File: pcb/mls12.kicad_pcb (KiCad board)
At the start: 4 copper layers, 80 x 40 mm, 0 parts

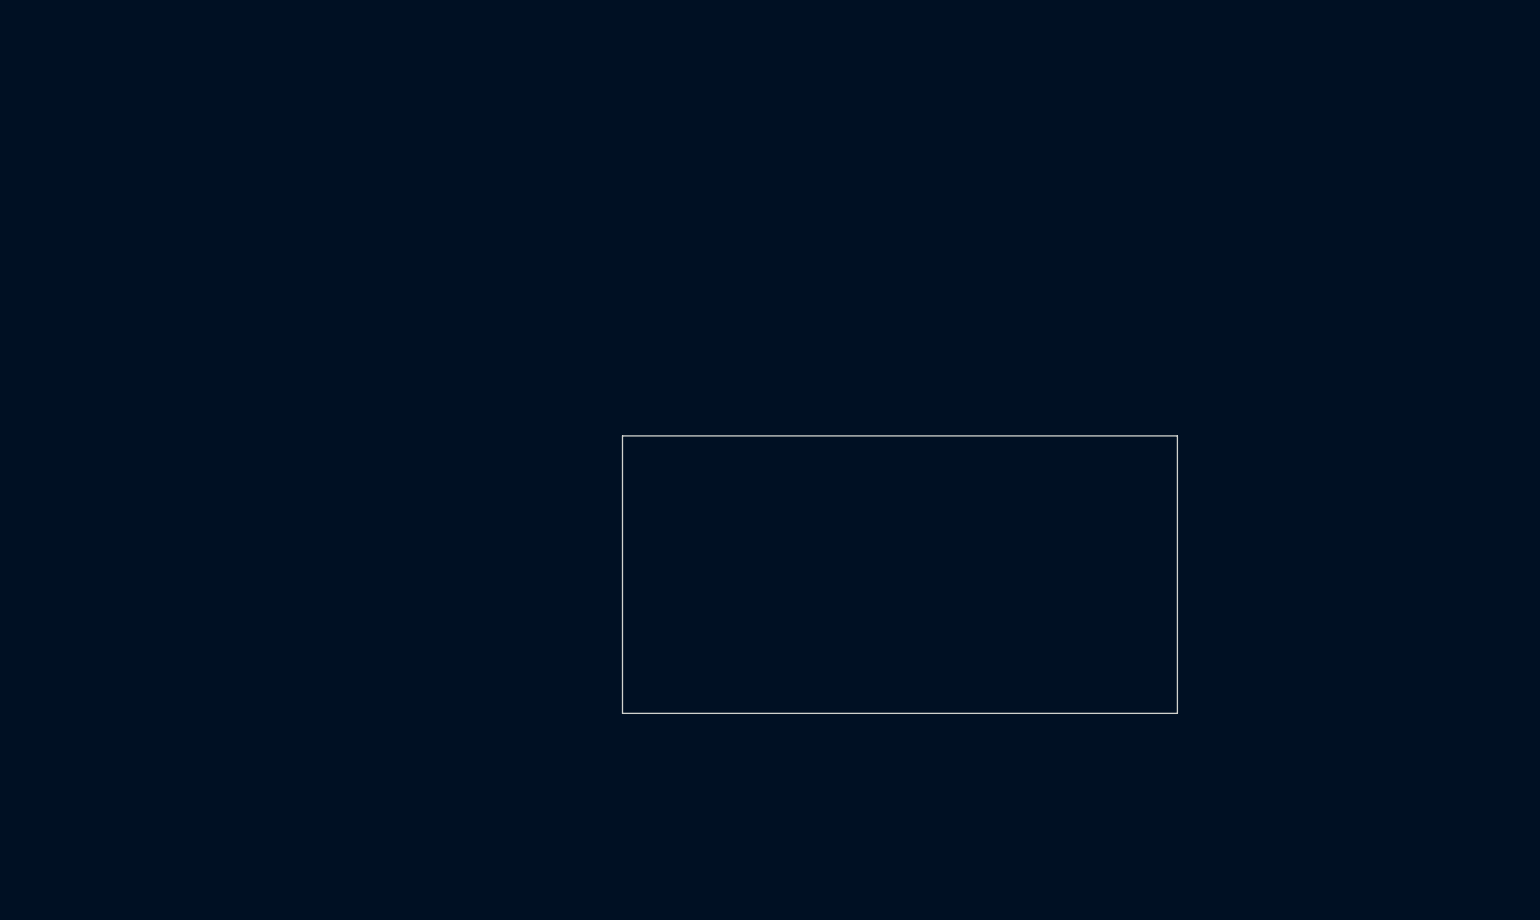
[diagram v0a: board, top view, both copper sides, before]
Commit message: Layout LED outputs, I2C connector
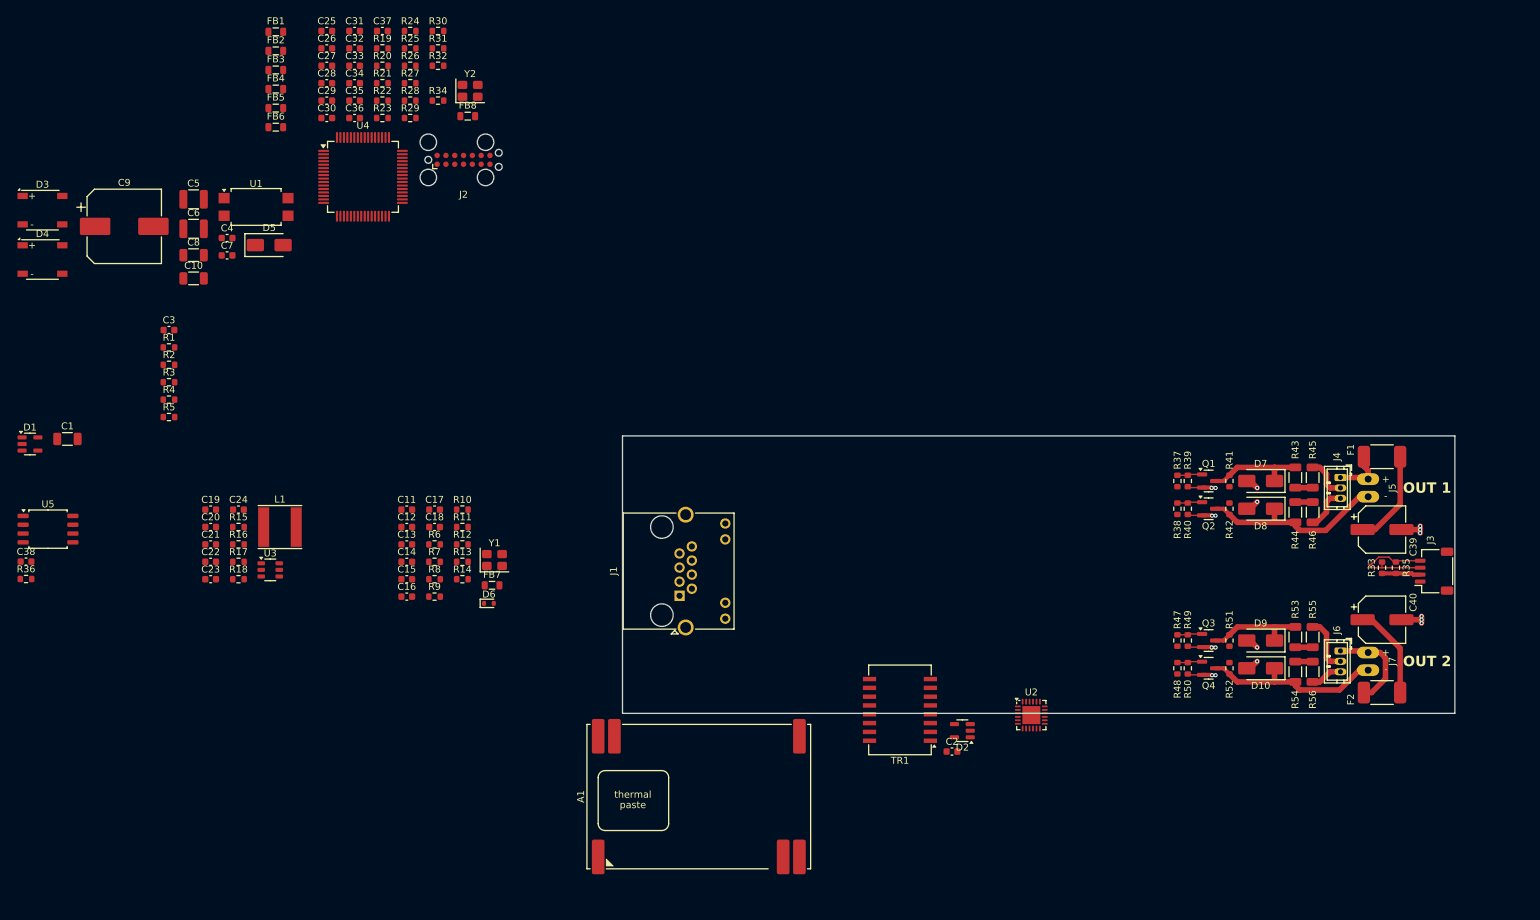
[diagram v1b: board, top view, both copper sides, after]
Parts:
- added A1: Ag5724-LPB, mls12:Ag5724-LPB, F.Cu at (121.0, 132.0)
- added C1: 1000pF/2kV, Capacitor_SMD:C_1206_3216Metric, F.Cu at (30.0, 80.4)
- added C10: 10uF/50V, Capacitor_SMD:C_1206_3216Metric, F.Cu at (48.2, 57.3)
- added C11: 22uF, Capacitor_SMD:C_0603_1608Metric, F.Cu at (78.9, 90.6)
- added C12: 0.1uF, Capacitor_SMD:C_0603_1608Metric, F.Cu at (78.9, 93.1)
- added C13: 0.1uF, Capacitor_SMD:C_0603_1608Metric, F.Cu at (78.9, 95.6)
- added C14: 0.1uF, Capacitor_SMD:C_0603_1608Metric, F.Cu at (78.9, 98.2)
- added C15: 22uF, Capacitor_SMD:C_0603_1608Metric, F.Cu at (78.9, 100.7)
- added C16: 2.2uF, Capacitor_SMD:C_0603_1608Metric, F.Cu at (78.9, 103.2)
- added C17: 10pF, Capacitor_SMD:C_0603_1608Metric, F.Cu at (82.9, 90.6)
- added C18: 10pF, Capacitor_SMD:C_0603_1608Metric, F.Cu at (82.9, 93.1)
- added C19: 4.7uF/35V, Capacitor_SMD:C_0603_1608Metric, F.Cu at (50.6, 90.6)
- added C2: 0.1uF, Capacitor_SMD:C_0603_1608Metric, F.Cu at (157.5, 125.5)
- added C20: 4.7uF/35V, Capacitor_SMD:C_0603_1608Metric, F.Cu at (50.6, 93.1)
- added C21: 0.1uF/50V, Capacitor_SMD:C_0603_1608Metric, F.Cu at (50.6, 95.6)
- added C22: 0.1uF, Capacitor_SMD:C_0603_1608Metric, F.Cu at (50.6, 98.2)
- added C23: 22uF, Capacitor_SMD:C_0603_1608Metric, F.Cu at (50.6, 100.7)
- added C24: 22uF, Capacitor_SMD:C_0603_1608Metric, F.Cu at (54.6, 90.6)
- added C25: 2.2uF, Capacitor_SMD:C_0603_1608Metric, F.Cu at (67.4, 21.6)
- added C26: 2.2uF, Capacitor_SMD:C_0603_1608Metric, F.Cu at (67.4, 24.1)
- added C27: 2.2uF, Capacitor_SMD:C_0603_1608Metric, F.Cu at (67.4, 26.6)
- added C28: 0.1uF, Capacitor_SMD:C_0603_1608Metric, F.Cu at (67.4, 29.1)
- added C29: 0.1uF, Capacitor_SMD:C_0603_1608Metric, F.Cu at (67.4, 31.7)
- added C3: 0.1uF, Capacitor_SMD:C_0603_1608Metric, F.Cu at (44.6, 64.7)
- added C30: 0.1uF, Capacitor_SMD:C_0603_1608Metric, F.Cu at (67.4, 34.2)
- added C31: 0.1uF, Capacitor_SMD:C_0603_1608Metric, F.Cu at (71.4, 21.6)
- added C32: 0.1uF, Capacitor_SMD:C_0603_1608Metric, F.Cu at (71.4, 24.1)
- added C33: 2.2uF, Capacitor_SMD:C_0603_1608Metric, F.Cu at (71.4, 26.6)
- added C34: 2.2uF, Capacitor_SMD:C_0603_1608Metric, F.Cu at (71.4, 29.1)
- added C35: 0.1uF, Capacitor_SMD:C_0603_1608Metric, F.Cu at (71.4, 31.7)
- added C36: 10pF, Capacitor_SMD:C_0603_1608Metric, F.Cu at (71.4, 34.2)
- added C37: 10pF, Capacitor_SMD:C_0603_1608Metric, F.Cu at (75.4, 21.6)
- added C38: 0.1uF, Capacitor_SMD:C_0603_1608Metric, F.Cu at (24.0, 98.1)
- added C39: 100uF/35V, Capacitor_SMD:CP_Elec_6.3x5.9, F.Cu at (219.5, 93.5)
- added C4: 10nF/100V, Capacitor_SMD:C_0603_1608Metric, F.Cu at (53.0, 51.5)
- added C40: 100uF/35V, Capacitor_SMD:CP_Elec_6.3x5.9, F.Cu at (219.5, 106.5)
- added C5: 4.7nF/2kV, Capacitor_SMD:C_1210_3225Metric, F.Cu at (48.2, 45.9)
- added C6: 4.7nF/2kV, Capacitor_SMD:C_1210_3225Metric, F.Cu at (48.2, 50.1)
- added C7: 0.1uF/50V, Capacitor_SMD:C_0603_1608Metric, F.Cu at (53.0, 54.0)
- added C8: 10uF/50V, Capacitor_SMD:C_1206_3216Metric, F.Cu at (48.2, 53.9)
- added C9: 560uF/35V, Capacitor_SMD:CP_Elec_10x10.5, F.Cu at (38.2, 49.8)
- added D1: ESDS312DBV, Package_TO_SOT_SMD:SOT-23-5, F.Cu at (24.6, 81.2)
- added D10: SMAJ24A, Diode_SMD:D_SMA, F.Cu at (202.0, 113.5)
- added D2: ESDS312DBV, Package_TO_SOT_SMD:SOT-23-5, F.Cu at (159.0, 122.5)
- added D3: LMB110S-TP, mls12:LMB110S-TP, F.Cu at (26.4, 47.5)
- added D4: LMB110S-TP, mls12:LMB110S-TP, F.Cu at (26.4, 54.6)
- added D5: SMAJ58A, Diode_SMD:D_SMA, F.Cu at (59.1, 52.5)
- added D6: 1N4148, Diode_SMD:D_SOD-523, F.Cu at (90.7, 104.1)
- added D7: SMAJ24A, Diode_SMD:D_SMA, F.Cu at (202.0, 86.5)
- added D8: SMAJ24A, Diode_SMD:D_SMA, F.Cu at (202.0, 90.5)
- added D9: SMAJ24A, Diode_SMD:D_SMA, F.Cu at (202.0, 109.5)
- added F1: 500mA/30V, mls12:SMD1812B050TF_30, F.Cu at (219.5, 83.0)
- added F2: 500mA/30V, mls12:SMD1812B050TF_30, F.Cu at (219.5, 117.0)
- added FB1: FerriteBead_Small, Inductor_SMD:L_0805_2012Metric, F.Cu at (60.0, 21.7)
- added FB2: FerriteBead_Small, Inductor_SMD:L_0805_2012Metric, F.Cu at (60.0, 24.5)
- added FB3: FerriteBead_Small, Inductor_SMD:L_0805_2012Metric, F.Cu at (60.0, 27.2)
- added FB4: FerriteBead_Small, Inductor_SMD:L_0805_2012Metric, F.Cu at (60.0, 30.0)
- added FB5: FerriteBead_Small, Inductor_SMD:L_0805_2012Metric, F.Cu at (60.0, 32.7)
- added FB6: FerriteBead_Small, Inductor_SMD:L_0805_2012Metric, F.Cu at (60.0, 35.5)
- added FB7: FerriteBead_Small, Inductor_SMD:L_0805_2012Metric, F.Cu at (91.2, 101.5)
- added FB8: FerriteBead_Small, Inductor_SMD:L_0805_2012Metric, F.Cu at (87.7, 33.9)
- added J1: MTJ-88ARX1-FSM-LG, Connector_RJ:RJ45_Amphenol_RJHSE538X, F.Cu at (118.2, 103.0)
- added J2: TC2070-FP, Connector:Tag-Connect_TC2070-IDC-FP_2x07_P1.27mm_Vertical, F.Cu at (87.1, 40.2)
- added J3: SM04B-SRSS-TB, Connector_JST:JST_SH_SM04B-SRSS-TB_1x04-1MP_P1.00mm_Horizontal, F.Cu at (227.0, 99.5)
- added J4: JST B3B-ZR, Connector_JST:JST_ZH_B3B-ZR_1x03_P1.50mm_Vertical, F.Cu at (213.5, 86.0)
- added J5: DC barrel plug, mls12:DC_Barrel_Plug_2.1x5.5mm, F.Cu at (217.5, 87.5)
- added J6: JST B3B-ZR, Connector_JST:JST_ZH_B3B-ZR_1x03_P1.50mm_Vertical, F.Cu at (213.5, 111.0)
- added J7: DC barrel plug, mls12:DC_Barrel_Plug_2.1x5.5mm, F.Cu at (217.5, 112.5)
- added L1: 33uH, Inductor_SMD:L_Taiyo-Yuden_NR-60xx, F.Cu at (60.6, 93.1)
- added Q1: DMG3406L, Package_TO_SOT_SMD:SOT-23, F.Cu at (194.5, 86.5)
- added Q2: DMG3406L, Package_TO_SOT_SMD:SOT-23, F.Cu at (194.5, 90.5)
- added Q3: DMG3406L, Package_TO_SOT_SMD:SOT-23, F.Cu at (194.5, 109.5)
- added Q4: DMG3406L, Package_TO_SOT_SMD:SOT-23, F.Cu at (194.5, 113.5)
- added R1: 220R, Resistor_SMD:R_0603_1608Metric, F.Cu at (44.6, 67.2)
- added R10: 33R, Resistor_SMD:R_0603_1608Metric, F.Cu at (86.9, 90.6)
- added R11: 0R, Resistor_SMD:R_0603_1608Metric, F.Cu at (86.9, 93.1)
- added R12: 0R, Resistor_SMD:R_0603_1608Metric, F.Cu at (86.9, 95.6)
- added R13: 1K, Resistor_SMD:R_0603_1608Metric, F.Cu at (86.9, 98.2)
- added R14: 10K, Resistor_SMD:R_0603_1608Metric, F.Cu at (86.9, 100.7)
- added R15: 0R, Resistor_SMD:R_0603_1608Metric, F.Cu at (54.6, 93.1)
- added R16: ~, Resistor_SMD:R_0603_1608Metric, F.Cu at (54.6, 95.6)
- added R17: 100K/1%, Resistor_SMD:R_0603_1608Metric, F.Cu at (54.6, 98.2)
- added R18: 32K/1%, Resistor_SMD:R_0603_1608Metric, F.Cu at (54.6, 100.7)
- added R19: 1K, Resistor_SMD:R_0603_1608Metric, F.Cu at (75.4, 24.1)
- added R2: 75, Resistor_SMD:R_0603_1608Metric, F.Cu at (44.6, 69.8)
- added R20: 33R, Resistor_SMD:R_0603_1608Metric, F.Cu at (75.4, 26.6)
- added R21: 33R, Resistor_SMD:R_0603_1608Metric, F.Cu at (75.4, 29.1)
- added R22: 10K, Resistor_SMD:R_0603_1608Metric, F.Cu at (75.4, 31.7)
- added R23: 33R, Resistor_SMD:R_0603_1608Metric, F.Cu at (75.4, 34.2)
- added R24: 33R, Resistor_SMD:R_0603_1608Metric, F.Cu at (79.4, 21.6)
- added R25: 33R, Resistor_SMD:R_0603_1608Metric, F.Cu at (79.4, 24.1)
- added R26: 33R, Resistor_SMD:R_0603_1608Metric, F.Cu at (79.4, 26.6)
- added R27: 0R, Resistor_SMD:R_0603_1608Metric, F.Cu at (79.4, 29.1)
- added R28: 100R, Resistor_SMD:R_0603_1608Metric, F.Cu at (79.4, 31.7)
- added R29: 100R, Resistor_SMD:R_0603_1608Metric, F.Cu at (79.4, 34.2)
- added R3: 75, Resistor_SMD:R_0603_1608Metric, F.Cu at (44.6, 72.3)
- added R30: 100R, Resistor_SMD:R_0603_1608Metric, F.Cu at (83.4, 21.6)
- added R31: 100R, Resistor_SMD:R_0603_1608Metric, F.Cu at (83.4, 24.1)
- added R32: 100R, Resistor_SMD:R_0603_1608Metric, F.Cu at (83.4, 26.6)
- added R33: 4K7, Resistor_SMD:R_0603_1608Metric, F.Cu at (219.5, 99.0)
- added R34: 100R, Resistor_SMD:R_0603_1608Metric, F.Cu at (83.4, 31.7)
- added R35: 4K7, Resistor_SMD:R_0603_1608Metric, F.Cu at (221.5, 99.0)
- added R36: 10K, Resistor_SMD:R_0603_1608Metric, F.Cu at (24.0, 100.6)
- added R37: 100R, Resistor_SMD:R_0603_1608Metric, F.Cu at (190.0, 86.5)
- added R38: 100R, Resistor_SMD:R_0603_1608Metric, F.Cu at (190.0, 90.5)
- added R39: 10K, Resistor_SMD:R_0603_1608Metric, F.Cu at (191.5, 86.5)
- added R4: 75, Resistor_SMD:R_0603_1608Metric, F.Cu at (44.6, 74.8)
- added R40: 10K, Resistor_SMD:R_0603_1608Metric, F.Cu at (191.5, 90.5)
- added R41: 10K, Resistor_SMD:R_0603_1608Metric, F.Cu at (197.5, 86.5)
- added R42: 10K, Resistor_SMD:R_0603_1608Metric, F.Cu at (197.5, 90.5)
- added R43: 3R/750mW, Resistor_SMD:R_1206_3216Metric, F.Cu at (207.0, 86.0)
- added R44: 3R/750mW, Resistor_SMD:R_1206_3216Metric, F.Cu at (207.0, 91.0)
- added R45: 3R/750mW, Resistor_SMD:R_1206_3216Metric, F.Cu at (209.5, 86.0)
- added R46: 3R/750mW, Resistor_SMD:R_1206_3216Metric, F.Cu at (209.5, 91.0)
- added R47: 100R, Resistor_SMD:R_0603_1608Metric, F.Cu at (190.0, 109.5)
- added R48: 100R, Resistor_SMD:R_0603_1608Metric, F.Cu at (190.0, 113.5)
- added R49: 10K, Resistor_SMD:R_0603_1608Metric, F.Cu at (191.5, 109.5)
- added R5: 75, Resistor_SMD:R_0603_1608Metric, F.Cu at (44.6, 77.3)
- added R50: 10K, Resistor_SMD:R_0603_1608Metric, F.Cu at (191.5, 113.5)
- added R51: 10K, Resistor_SMD:R_0603_1608Metric, F.Cu at (197.5, 109.5)
- added R52: 10K, Resistor_SMD:R_0603_1608Metric, F.Cu at (197.5, 113.5)
- added R53: 3R/750mW, Resistor_SMD:R_1206_3216Metric, F.Cu at (207.0, 109.0)
- added R54: 3R/750mW, Resistor_SMD:R_1206_3216Metric, F.Cu at (207.0, 114.0)
- added R55: 3R/750mW, Resistor_SMD:R_1206_3216Metric, F.Cu at (209.5, 109.0)
- added R56: 3R/750mW, Resistor_SMD:R_1206_3216Metric, F.Cu at (209.5, 114.0)
- added R6: 6K49/1%, Resistor_SMD:R_0603_1608Metric, F.Cu at (82.9, 95.6)
- added R7: 33R, Resistor_SMD:R_0603_1608Metric, F.Cu at (82.9, 98.2)
- added R8: 33R, Resistor_SMD:R_0603_1608Metric, F.Cu at (82.9, 100.7)
- added R9: 33R, Resistor_SMD:R_0603_1608Metric, F.Cu at (82.9, 103.2)
- added TR1: 7490120110, mls12:7490120110, F.Cu at (150.0, 119.5)
- added U1: DPC817S-C-TR, mls12:DPC817S-C-TR, F.Cu at (57.2, 47.0)
- added U2: KSZ8081RNA, Package_DFN_QFN:QFN-24-1EP_4x4mm_P0.5mm_EP2.6x2.6mm, F.Cu at (168.9, 120.2)
- added U3: LMR51606XDBVR, mls12:LMR51606_SOT-23-6, F.Cu at (59.2, 99.3)
- added U4: STM32H563RIT6, Package_QFP:LQFP-64_10x10mm_P0.5mm, F.Cu at (72.6, 42.6)
- added U5: W25Q16JVSS, Package_SO:SOIC-8_5.3x5.3mm_P1.27mm, F.Cu at (27.2, 93.4)
- added Y1: 25MHz, Crystal:Crystal_SMD_3225-4Pin_3.2x2.5mm, F.Cu at (91.5, 97.9)
- added Y2: 25MHz, Crystal:Crystal_SMD_3225-4Pin_3.2x2.5mm, F.Cu at (88.0, 30.2)
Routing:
- net GND: track 0.00 -> 30.7 mm, vias 0 -> 18
- net /LED output 1/LED_CW-: track 0.00 -> 28.1 mm
- net +24V: track 0.00 -> 27.3 mm
- net /LED output 2/LED_CW-: track 0.00 -> 27.3 mm
- net /LED output 2/LED_WW-: track 0.00 -> 14.3 mm
- net /LED output 1/LED_WW-: track 0.00 -> 14.3 mm
- net /LED output 2/LED+: track 0.00 -> 13.9 mm
- net /MCU/SDA: track 0.00 -> 8.33 mm
- net /MCU/SCL: track 0.00 -> 8.30 mm
- net Net-(J6-Pin_2): track 0.00 -> 8.11 mm
- net /LED output 1/LED+: track 0.00 -> 7.58 mm
- net Net-(J4-Pin_3): track 0.00 -> 6.31 mm
- net Net-(J4-Pin_2): track 0.00 -> 6.11 mm
- net +3.3V: track 0.00 -> 5.57 mm
- net Net-(J6-Pin_3): track 0.00 -> 4.61 mm
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- added copper zone on In1.Cu, net GND
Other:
- board size 80 x 40 mm -> 120 x 40 mm
- board text added: "OUT 1"
- board text added: "OUT 2"

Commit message: First Ethernet frontend layout
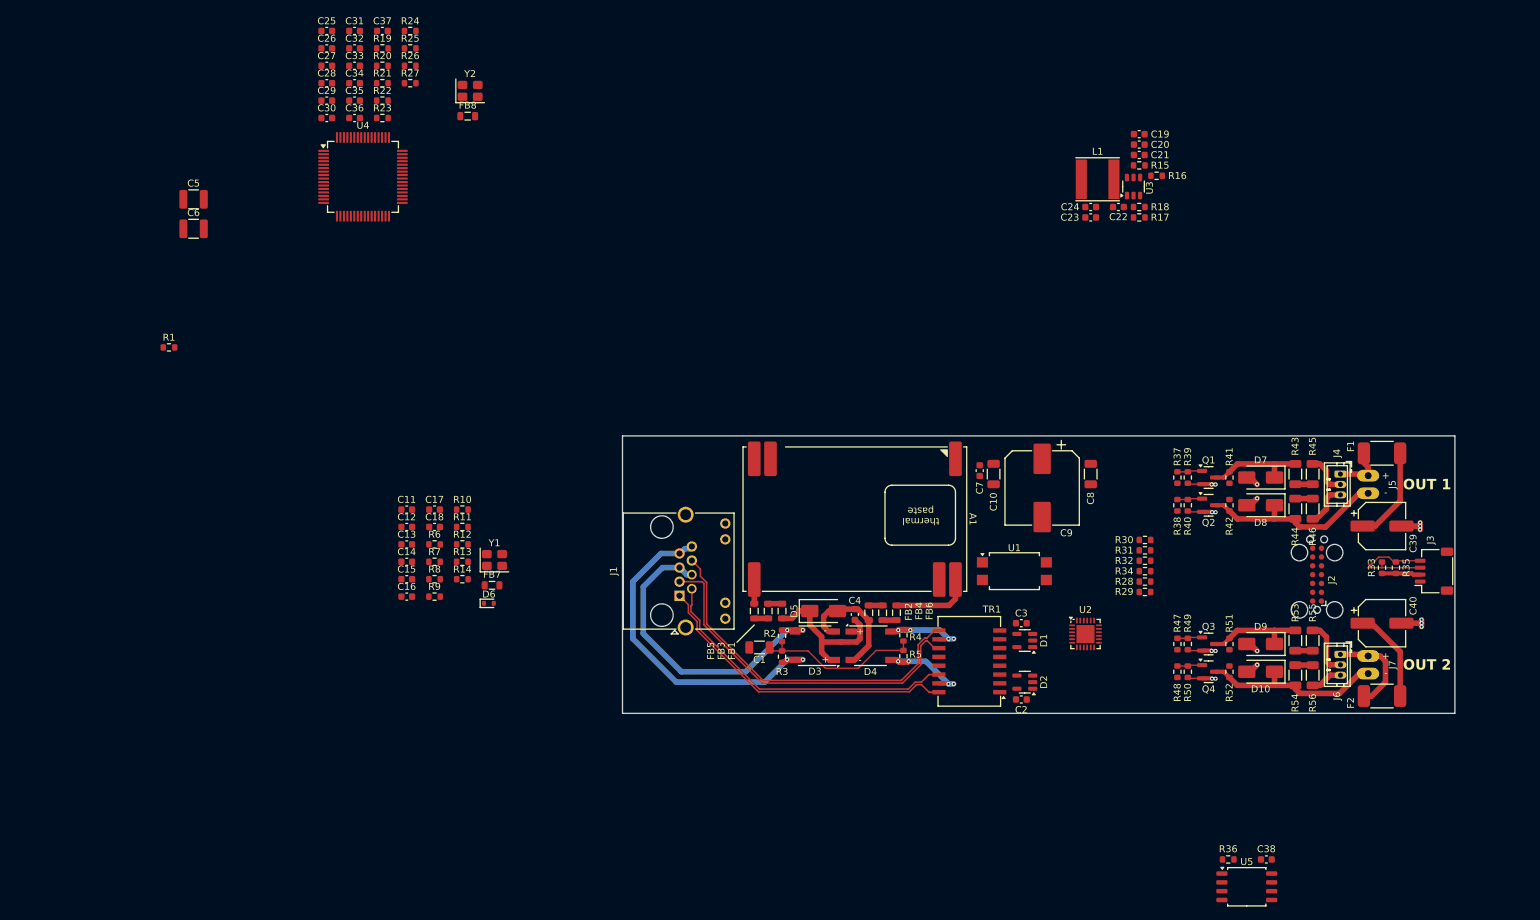
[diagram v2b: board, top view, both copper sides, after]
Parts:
- moved C38 183.9 mm to (202.8, 141.1), turned to 180 degrees
- moved U5 180.4 mm to (200.0, 145.0)
- moved R36 178.0 mm to (197.3, 141.1), turned to 180 degrees
- moved D1 146.2 mm to (168.0, 109.5), turned to 180 degrees
- moved C21 145.2 mm to (184.5, 39.5)
- moved C20 144.8 mm to (184.5, 38.0)
- moved C19 144.4 mm to (184.5, 36.5)
- moved R16 142.6 mm to (187.0, 42.5)
- moved C22 140.5 mm to (181.5, 47.0), turned to 180 degrees
- moved R18 140.5 mm to (184.5, 47.0), turned to 180 degrees
- moved R15 139.9 mm to (184.5, 41.0)
- moved R17 139.0 mm to (184.5, 48.5)
- moved C9 137.6 mm to (170.5, 87.5), turned to -90 degrees
- moved C23 137.2 mm to (177.5, 48.5)
- moved J2 136.8 mm to (210.1, 100.0), turned to 90 degrees
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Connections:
- net /ETH-CONN/RX+ renamed /ETH-CONN/MDI_RD+
- net /ETH-CONN/RX- renamed /ETH-CONN/MDI_RD-
- net /ETH-CONN/TX+ renamed /ETH-CONN/MDI_TD+
- net /ETH-CONN/TX- renamed /ETH-CONN/MDI_TD-
- net Net-(TR1-RX+) renamed /ETH-CONN/MDI_RX+
- net Net-(TR1-RX-) renamed /ETH-CONN/MDI_RX-
- net Net-(TR1-TX+) renamed /ETH-CONN/MDI_TX+
- net Net-(TR1-TX-) renamed /ETH-CONN/MDI_TX-
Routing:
- net /ETH-CONN/MDI_RX+: track 0.00 -> 51.5 mm
- net /ETH-CONN/MDI_RX-: track 0.00 -> 51.5 mm
- net /ETH-CONN/V_{INB}: track 0.00 -> 50.5 mm, vias 0 -> 2
- net /ETH-CONN/V_{INA}: track 0.00 -> 46.3 mm, vias 0 -> 2
- net /ETH-CONN/MDI_TX+: track 0.00 -> 45.4 mm
- net /ETH-CONN/MDI_TX-: track 0.00 -> 45.3 mm
- net Net-(C1-Pad1): track 0.00 -> 24.3 mm
- net Net-(D3-+): track 0.00 -> 23.6 mm
- net Net-(D3--): track 0.00 -> 18.1 mm
- net /ETH-CONN/V_{INC}: track 0.00 -> 13.5 mm, vias 0 -> 4
- net /ETH-CONN/V_{IND}: track 0.00 -> 13.0 mm, vias 0 -> 4
- net Net-(A1-V_{IN-}): track 0.00 -> 11.7 mm
- net Net-(A1-V_{IN+}): track 0.00 -> 3.49 mm
- net Net-(FB4-Pad2): track 0.00 -> 2.00 mm
- net Net-(FB3-Pad2): track 0.00 -> 2.00 mm
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
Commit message: Initial RMII, MDIO routing
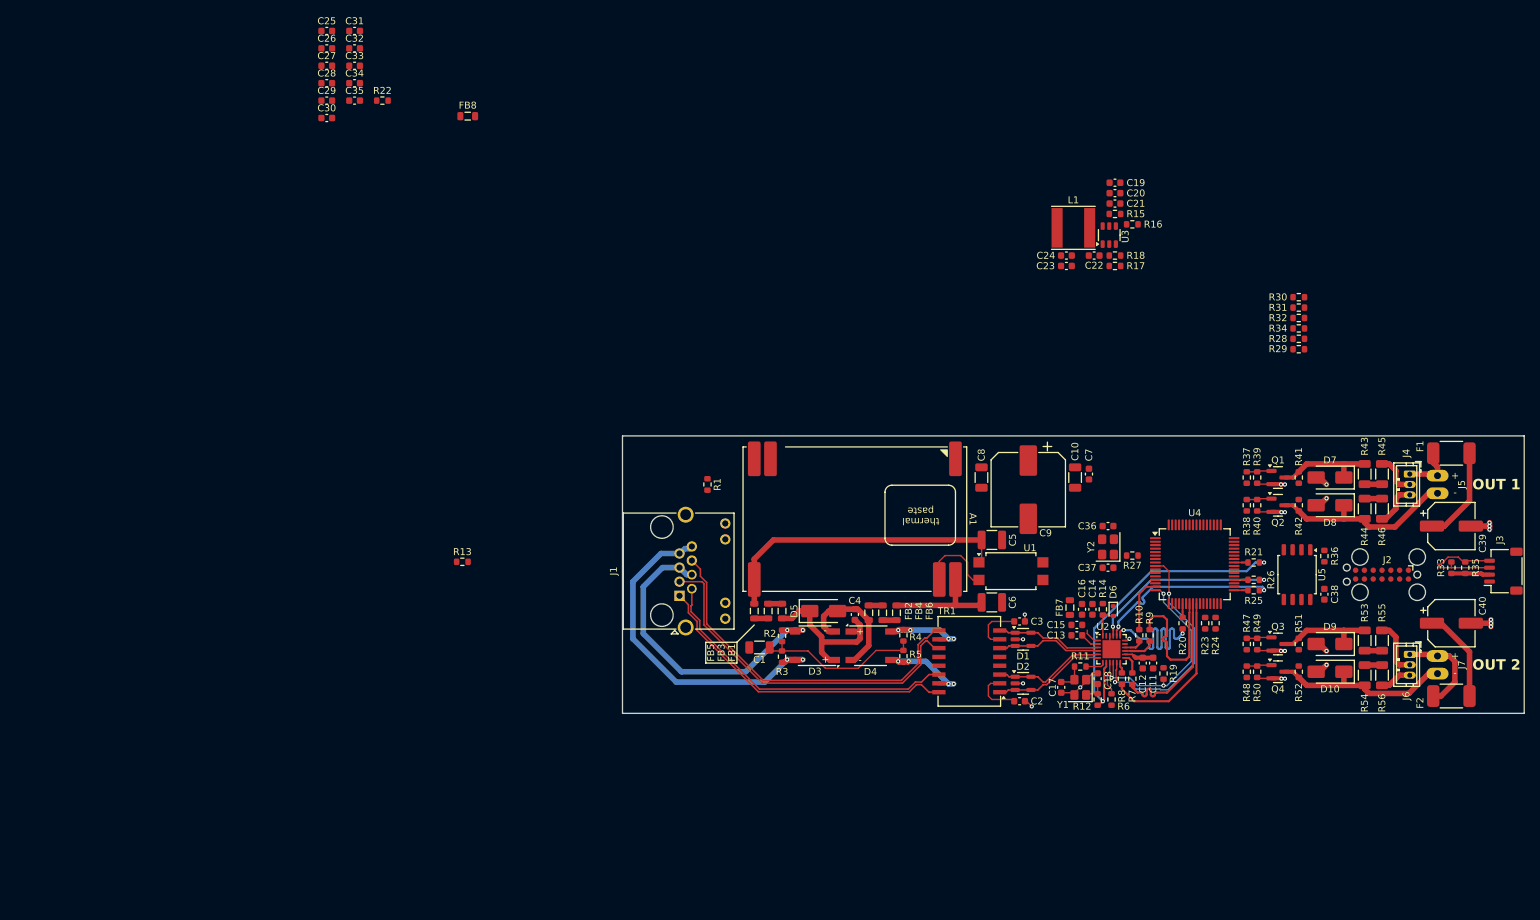
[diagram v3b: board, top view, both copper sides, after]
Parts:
- moved R25 144.5 mm to (201.0, 102.2)
- moved R19 144.2 mm to (188.0, 114.2), turned to -90 degrees
- moved R24 144.1 mm to (195.5, 107.0), turned to -90 degrees
- moved R21 143.4 mm to (201.0, 98.2)
- moved R26 142.4 mm to (201.0, 100.8)
- moved R20 140.6 mm to (190.8, 107.0), turned to -90 degrees
- moved R23 139.2 mm to (194.0, 107.0), turned to -90 degrees
- moved U4 132.3 mm to (192.5, 98.5)
- moved C37 130.1 mm to (180.0, 99.0)
- moved C6 127.1 mm to (163.2, 104.0)
- moved C5 125.1 mm to (163.2, 95.0)
- moved R27 124.4 mm to (183.5, 97.2), turned to 180 degrees
- moved C36 123.5 mm to (180.0, 93.0)
- moved Y2 113.1 mm to (180.0, 96.0), turned to 90 degrees
- moved C11 109.9 mm to (186.5, 112.8), turned to -90 degrees
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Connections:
- D1 pad 1: unconnected-(D1-NC-Pad1) -> /ETH-CONN/MDI_RD-
- D1 pad 3: unconnected-(D1-NC-Pad3) -> /ETH-CONN/MDI_RD+
- D1 pad 4: /ETH-CONN/MDI_RD- -> /ETH-CONN/MDI_RD+
- D1 pad 5: /ETH-CONN/MDI_RD+ -> /ETH-CONN/MDI_RD-
- D2 pad 1: unconnected-(D2-NC-Pad1) -> /ETH-CONN/MDI_TD-
- D2 pad 3: unconnected-(D2-NC-Pad3) -> /ETH-CONN/MDI_TD+
- D2 pad 4: /ETH-CONN/MDI_TD- -> /ETH-CONN/MDI_TD+
- D2 pad 5: /ETH-CONN/MDI_TD+ -> /ETH-CONN/MDI_TD-
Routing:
- net /ETH-PHY/CLK_25MHZ: track 0.00 -> 46.9 mm, vias 0 -> 2
- net Net-(A1-V_{IN+}): track 3.49 -> 43.7 mm
- net /ETH-PHY/MDC: track 0.00 -> 33.5 mm, vias 0 -> 2
- net /ETH-PHY/MDIO: track 0.00 -> 29.4 mm, vias 0 -> 3
- net /ETH-PHY/TXD_{1}: track 0.00 -> 27.5 mm, vias 0 -> 2
- net /ETH-PHY/TXD_{0}: track 0.00 -> 27.3 mm, vias 0 -> 2
- net /ETH-PHY/TX_EN: track 0.00 -> 27.2 mm, vias 0 -> 2
- net /ETH-PHY/RXD_{1}: track 0.00 -> 23.9 mm
- net /ETH-PHY/RXD_{0}: track 0.00 -> 22.4 mm
- net /ETH-PHY/CRS_DV: track 0.00 -> 21.7 mm
- net /ETH-CONN/MDI_TD-: track 0.00 -> 16.3 mm
- net /ETH-CONN/MDI_TD+: track 0.00 -> 16.3 mm
- net /ETH-CONN/MDI_RD+: track 0.00 -> 15.2 mm
- net /ETH-CONN/MDI_RD-: track 0.00 -> 15.2 mm
- net GND: track 30.7 -> 44.3 mm, vias 18 -> 23
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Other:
- board size 120 x 40 mm -> 130 x 40 mm
